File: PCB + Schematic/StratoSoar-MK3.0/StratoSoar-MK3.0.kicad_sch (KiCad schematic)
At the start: 83 parts, among them J1 Power, J11 Signal, J12 Rudder, J2 Battery, J3 USB-C, J4 J Link, J5 Antenna, J6 Rudder, J8 Button, Q1 DMN1019USN-13, Q2 DMN1019USN-13, Q7 BSS138, Q8 BSS138, Q9 BSS138, SW1 RESET, SW2 PWR_SW, SW5 EEPROM, U1 Ra-01, U10 ICM-20948, U11 DSK321STD, U12 XC6206P332MR-G, U2 ATSAMD21G18A-A, U4 ATGM336H, U5 BME280, U6 AT24C512C-SSHD-T, U7 AT24CS32-STUM, U9 CJ6206B18M

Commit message: PCB
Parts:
- removed J11: Signal, Connector_PinHeader_2.54mm:PinHeader_1x11_P2.54mm_Vertical, symbol Connector_Generic:Conn_01x11
- added J7: Signal, Connector_PinHeader_2.54mm:PinHeader_1x09_P2.54mm_Vertical, symbol Connector_Generic:Conn_01x09
- added R15, R16: 1.8 K, Resistor_SMD:R_0603_1608Metric, symbol Device:R_Small
- D1: value PWR_RED -> ERR_RED
- JP2: value PWR_LED_EN -> ERR_LED_EN
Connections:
- net A0 is gone; now on net BATT: U2.3 (PA02)
- net D0 is gone; now on net RX: U2.16 (PA11)
- net D1 is gone; now on net TX: U2.15 (PA10)
- net D13 is gone; now on net LED: U2.26 (PA17)
- net D5 is gone; now on net DIO0: U2.24 (PA15)
- net D6 is gone; now on net LORA_RST: U2.29 (PA20)
- net D7 is gone; now on net R_FET: U2.30 (PA21)
- net D8 is gone; now on net L_FET: U2.11 (PA06)
- net L is gone; now on net LEFT: J6.3 (Pin_3)
- net R is gone; now on net RIGHT: J12.3 (Pin_3)
- net +3.3V: now also R15.2, R16.2; no longer JP2.2 (B), U4.5 (EN)
- net A1: now also J7.9 (Pin_9)
- net D2: now also J7.8 (Pin_8)
- net D3: now also J7.7 (Pin_7)
- net GND: now also J8.1 (Pin_1), J7.1 (Pin_1); no longer J8.2 (Pin_2)
- net GPS_SCL: now also R15.1
- net GPS_SDA: now also R16.1
- net MISO: now also J7.4 (Pin_4)
- net MOSI: now also J7.5 (Pin_5)
- net SCK: now also J7.6 (Pin_6)
- net SCL: now also J7.3 (Pin_3)
- net SDA: now also J7.2 (Pin_2)
- net DIO0: now reaches U1.5 (DIO0)
- net D10 renamed LEFT
- net D11 renamed GPS_EN
- net GPS_EN: now also U4.5 (EN)
- net D12 renamed ERR
- net ERR: now also JP2.2 (B)
- net D4 renamed BTN
- net BTN: now also J8.2 (Pin_2)
- net D9 renamed RIGHT
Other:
- note added: "EDIT GPS BREAKOUT TO HAVE I2C PULLUP RESISTORS"
- note removed: "DOES THE IMU HAVE BUILT IN I2C PULLUP RESISTORS"
- moved on the sheet: AE3, BT1, C1, C17, C18, C2, D3, J5, J8, L3, R10, U1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

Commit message: Finished all connections on PCB
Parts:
- renumbered Q9 to #Q9, R20 to #R20, R22 to #R22
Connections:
- net D3: now also J7.4 (Pin_4); no longer J7.7 (Pin_7)
- net MISO: now also J7.7 (Pin_7); no longer J7.4 (Pin_4)
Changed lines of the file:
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@@
 	(global_label "D3"
 		(shape input)
-		(at 387.35 189.23 0)
+		(at 387.35 196.85 0)
 		(fields_autoplaced yes)
 		(effects
@@
 		)
 		(property "Intersheetrefs" "${INTERSHEET_REFS}"
-			(at 392.8147 189.23 0)
+			(at 392.8147 196.85 0)
 			(effects
 				(font
@@
 	(global_label "MISO"
 		(shape input)
-		(at 387.35 196.85 0)
+		(at 387.35 189.23 0)
 		(fields_autoplaced yes)
 		(effects
@@
 		)
 		(property "Intersheetrefs" "${INTERSHEET_REFS}"
-			(at 394.9314 196.85 0)
+			(at 394.9314 189.23 0)
 			(effects
 				(font
@@
 		(dnp no)
 		(fields_autoplaced yes)
-		(property "Reference" "Q9"
+		(property "Reference" "#Q9"
 			(at 97.79 93.98 90)
 			(effects
@@
 			(project "StratoSoar-MK3.0"
 				(path "/a5ed86dc-e941-4edd-8d1d-eae06db8d6f6"
-					(reference "Q9")
+					(reference "#Q9")
 					(unit 1)
 				)
@@
 		(dnp no)
 		(fields_autoplaced yes)
-		(property "Reference" "R20"
+		(property "Reference" "#R20"
 			(at 88.9 82.5499 0)
 			(effects
@@
 			(project "StratoSoar-MK3.0"
 				(path "/a5ed86dc-e941-4edd-8d1d-eae06db8d6f6"
-					(reference "R20")
+					(reference "#R20")
 					(unit 1)
 				)
@@
 		(dnp no)
 		(fields_autoplaced yes)
-		(property "Reference" "R22"
+		(property "Reference" "#R22"
 			(at 110.49 83.8199 0)
 			(effects
@@
 			(project "StratoSoar-MK3.0"
 				(path "/a5ed86dc-e941-4edd-8d1d-eae06db8d6f6"
-					(reference "R22")
+					(reference "#R22")
 					(unit 1)
 				)

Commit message: Mostly silkscreen
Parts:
- renumbered AE3 to AE1, C17 to C1, C9 to C10, C10 to C11, C5 to C12, C3 to C13, C12 to C14, C7 to C15, C6 to C16, C4 to C17, C2 to C18, C1 to C19, C15 to C2, C24 to C21, C11 to C22, C30 to C23, C27 to C24, C18 to C3, C14 to C4, C23 to C5, C25 to C6, C8 to C7, C26 to C8, C13 to C9, D3 to D1, D4 to D2, D1 to D3, J7 to J1, J1 to J2, J8 to J3, J3 to J4, J4 to J5, J5 to J6, J2 to J7, J12 to J8, J6 to J9, JP3 to JP1, L3 to L1, Q8 to Q1, Q7 to Q2, Q1 to Q3, Q2 to Q4, R16 to R1, R4 to R10, R2 to R11, R6 to R12, R5 to R13, R3 to R14, R9 to R15, R8 to R16, R12 to R17, R14 to R19, R10 to R2, R21 to R20, R17 to R3, R19 to R4, R15 to R5, R7 to R6, R11 to R7, R13 to R8, R1 to R9, SW5 to SW1, SW1 to SW2, SW2 to SW3, U6 to U1, U1 to U10, U4 to U2, U7 to U3, U5 to U4, U11 to U5, U9 to U6, U10 to U7, U2 to U8, U12 to U9

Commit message: Silkscreen!
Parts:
- removed JP2: ERR_LED_EN, Jumper:SolderJumper-2_P1.3mm_Open_RoundedPad1.0x1.5mm, symbol Jumper:SolderJumper_2_Open
- JP1: value LED_EN -> ALWAYS_ON; now left out of the parts list
- renumbered J6 to AE2
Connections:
- net +BATT: now also JP1.2 (B)
- net ERR: now also R14.2
- net LED: now also R10.2; no longer JP1.2 (B)
- net VCC: now also JP1.1 (A)
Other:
- moved on the sheet: D2, D3, J5, R10, R14

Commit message: Actually finished board for real?
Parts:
- C12, C16, C7: LCSC C14663 -> C1525
- C14, C9: footprint Capacitor_SMD:C_0402_1005Metric -> Capacitor_SMD:C_0603_1608Metric
- R2: LCSC C25077 -> C11702
- U1: value AT24C512C-SSHD-T -> AT24C512C-SSHM-T; LCSC C615466 -> C54668
- U2: LCSC C5117921 -> C90770
- U3: value AT24CS32-STUM -> BL24C32F-RRRC; LCSC (none) -> C5185883

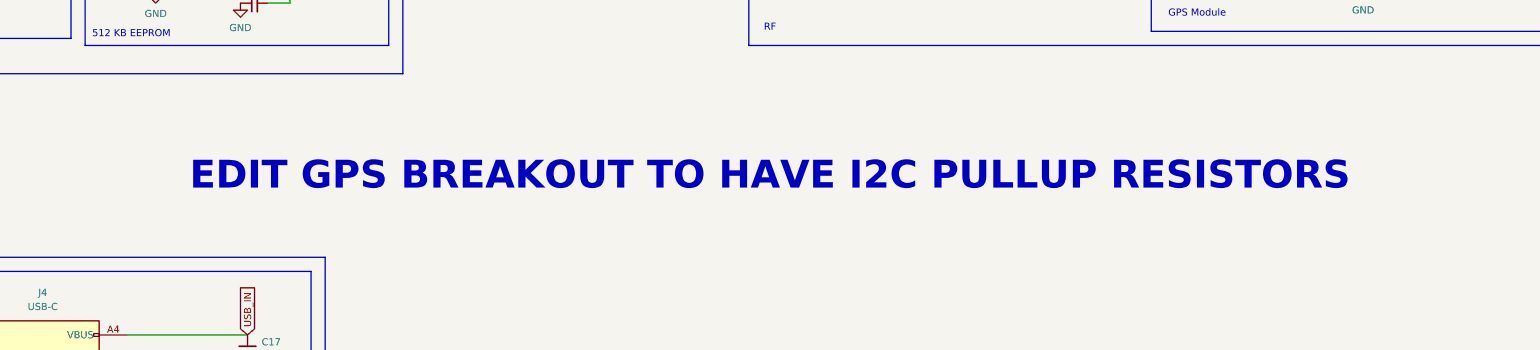
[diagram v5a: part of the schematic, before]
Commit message: GPS, IMU
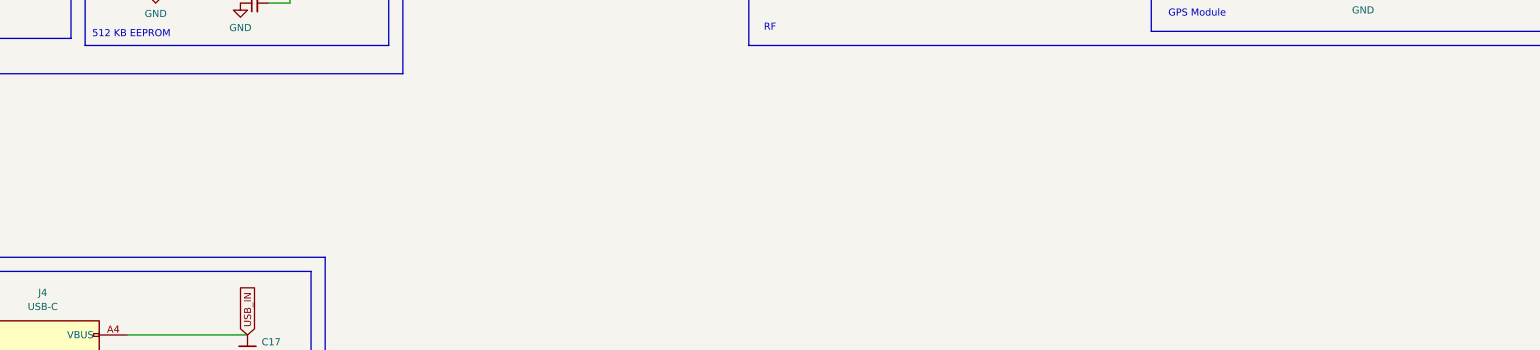
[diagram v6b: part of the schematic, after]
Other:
- note removed: "EDIT GPS BREAKOUT TO HAVE I2C PULLUP RESISTORS"
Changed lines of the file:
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@@
-		)
-	)
-	(text "EDIT GPS BREAKOUT TO HAVE I2C PULLUP RESISTORS"
-		(exclude_from_sim no)
-		(at 243.84 128.905 0)
-		(effects
-			(font
-				(size 5 5)
-				(thickness 1)
-				(bold yes)
-			)
 		)
 	)

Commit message: Commit
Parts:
- AE1: value 1575AT43A0040001E -> GPS1003; footprint 1575AT43A0040E:ANT_1575AT_JOT-L -> RF_Antenna:GPS1003
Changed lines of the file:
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@@
 			)
 		)
-		(property "Value" "1575AT43A0040001E"
+		(property "Value" "GPS1003"
 			(at 369.57 33.0199 0)
 			(effects
@@
 			)
 		)
-		(property "Footprint" "1575AT43A0040E:ANT_1575AT_JOT-L"
+		(property "Footprint" "RF_Antenna:GPS1003"
 			(at 361.95 29.845 0)
 			(effects
